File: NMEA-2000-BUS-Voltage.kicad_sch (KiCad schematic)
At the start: 12 parts, among them J2 Conn_01x07, J3 Conn_01x04_Socket, SW1 SW_Push, U1 WeMos_D1_mini, U2 LM7805_TO220

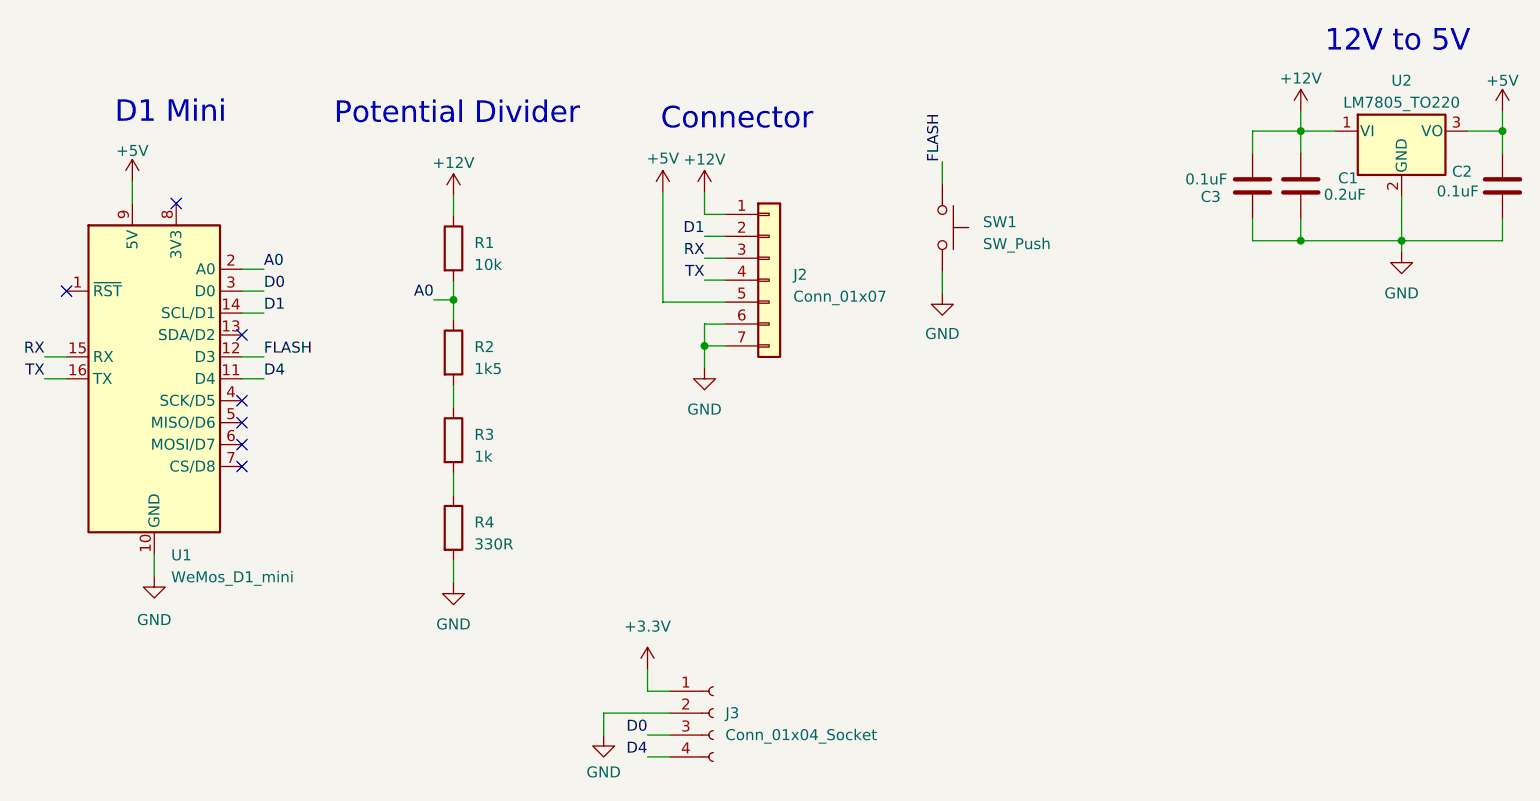
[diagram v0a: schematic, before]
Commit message: Added Relay Connector
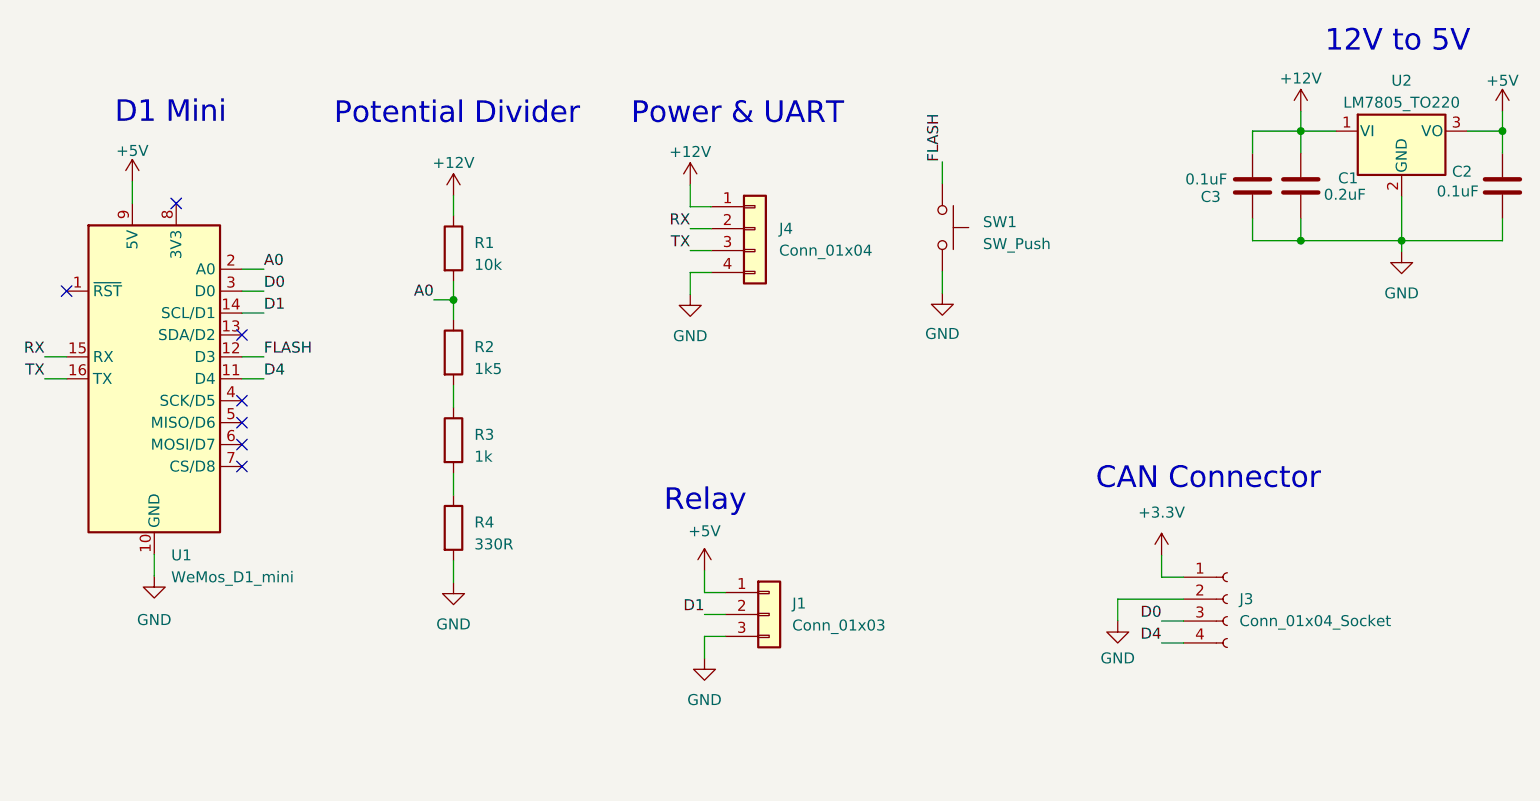
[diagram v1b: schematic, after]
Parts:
- removed J2: Conn_01x07, symbol Connector_Generic:Conn_01x07
- added J1: Conn_01x03, symbol Connector_Generic:Conn_01x03
- added J4: Conn_01x04, symbol Connector_Generic:Conn_01x04
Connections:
- net +12V: now also J4.1 (Pin_1)
- net +5V: now also J1.1 (Pin_1)
- net D1: now also J1.2 (Pin_2)
- net GND: now also J1.3 (Pin_3), J4.4 (Pin_4)
- net RX: now also J4.2 (Pin_2)
- net TX: now also J4.3 (Pin_3)
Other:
- note added: "CAN Connector"
- note added: "Power & UART"
- note added: "Relay"
- note removed: "Connector"
- moved on the sheet: J3

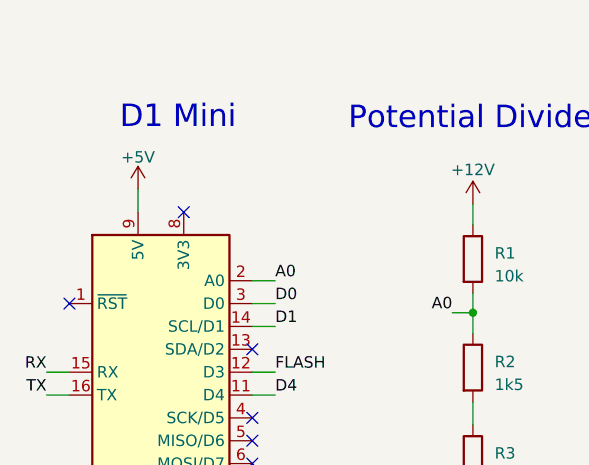
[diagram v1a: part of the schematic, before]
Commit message: Added 3.3V to D1
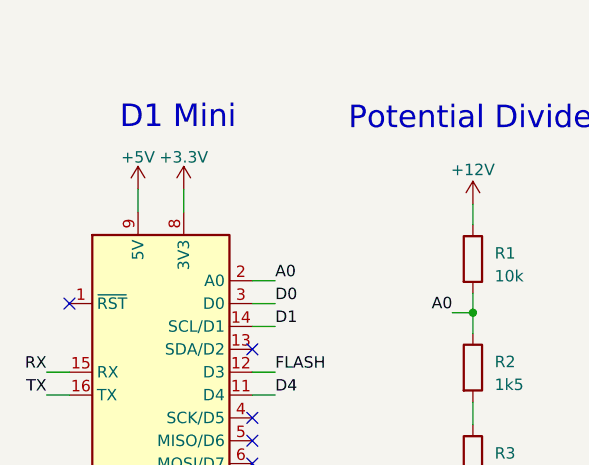
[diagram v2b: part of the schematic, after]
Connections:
- net +3.3V: now also U1.8 (3V3)
- no-connect marks 7 -> 6
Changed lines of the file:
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@@
   (no_connect (at 46.736 62.357))
   (no_connect (at 46.736 57.277))
-  (no_connect (at 39.116 34.417))
   (wire (pts (xy 181.102 38.735) (xy 181.102 40.005))
     (stroke (width 0) (type default))
@@
   )
   (wire (pts (xy 192.786 38.735) (xy 192.786 36.195))
+    (stroke (width 0) (type default))
+  )
+  (wire (pts (xy 39.116 31.877) (xy 39.116 34.417))
     (stroke (width 0) (type default))
   )
@@
         )
       )
+    )
+  )
+  (symbol (lib_id "power:+3.3V") (at 39.116 31.877 0) (unit 1)
+    (in_bom yes) (on_board yes) (dnp no)
+    (property "Reference" "#PWR011" (at 39.116 35.687 0)
+      (effects (font (size 1.27 1.27)) hide)
+    )
+    (property "Value" "+3.3V" (at 39.116 28.321 0)
+      (effects (font (size 1.27 1.27)))
+    )
+    (property "Footprint" "" (at 39.116 31.877 0)
+      (effects (font (size 1.27 1.27)) hide)
+    )
+    (property "Datasheet" "" (at 39.116 31.877 0)
+      (effects (font (size 1.27 1.27)) hide)
+    )
+    (pin "1")
+    (instances
+      (project "NMEA-2000-BUS-Voltage"
+        (path "/f79966b4-4927-4ec7-886d-17305cb22602"
+          (reference "#PWR011") (unit 1)
+        )
+      )
